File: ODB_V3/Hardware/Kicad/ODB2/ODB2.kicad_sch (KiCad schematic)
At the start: 95 parts, among them U1 STM32F412ZGTx, Y1 ABM8G-25.000MHZ-18-D2Y-T

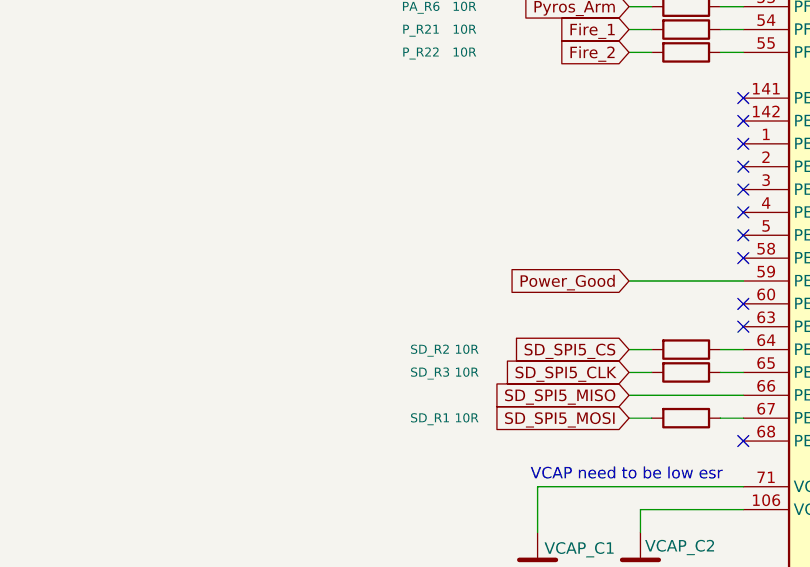
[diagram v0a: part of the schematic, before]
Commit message: feat: add good power input to stm32 + add pull-up 3v3 to good power
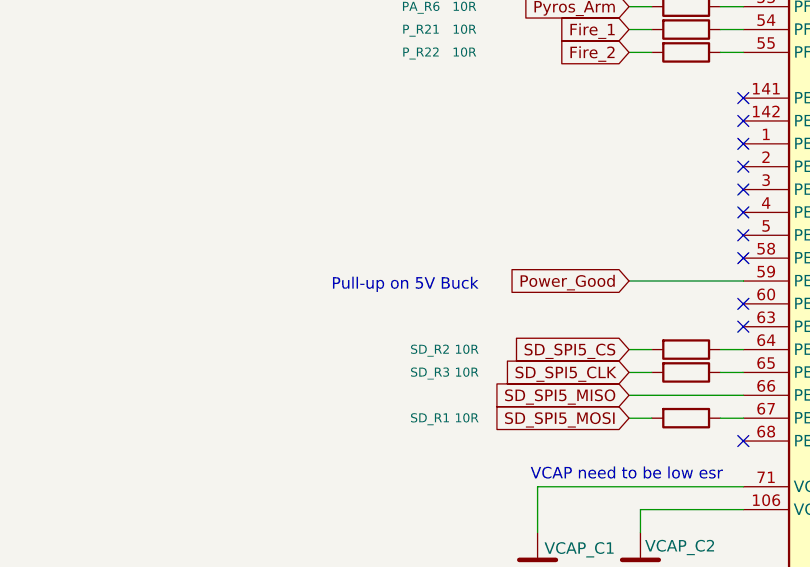
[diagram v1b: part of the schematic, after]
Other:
- note added: "Pull-up on 5V Buck"
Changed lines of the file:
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@@
+		)
+	)
+	(text "Pull-up on 5V Buck"
+		(exclude_from_sim no)
+		(at 132.588 191.008 0)
+		(effects
+			(font
+				(size 1.27 1.27)
+			)
 		)
 	)

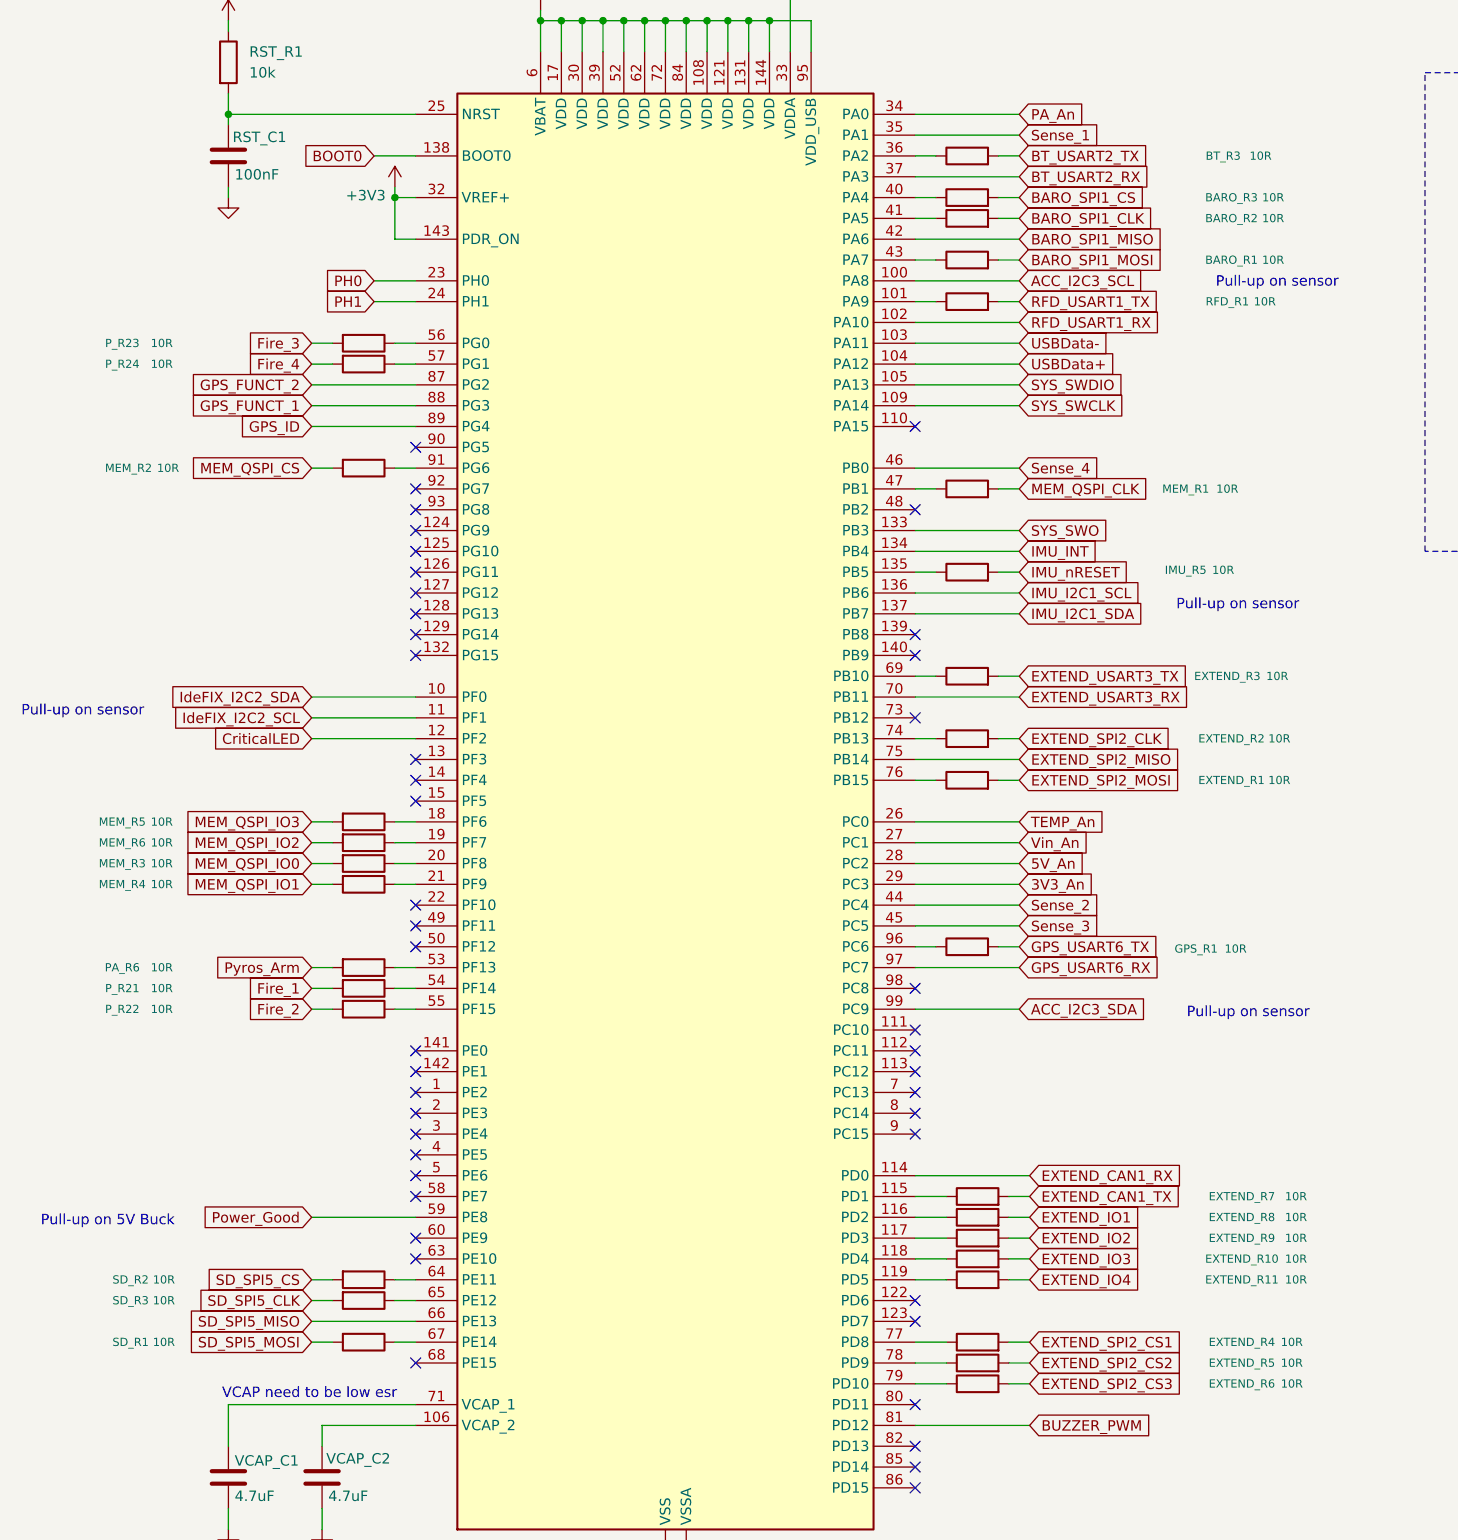
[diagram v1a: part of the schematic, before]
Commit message: fix: reoganised components on pcb
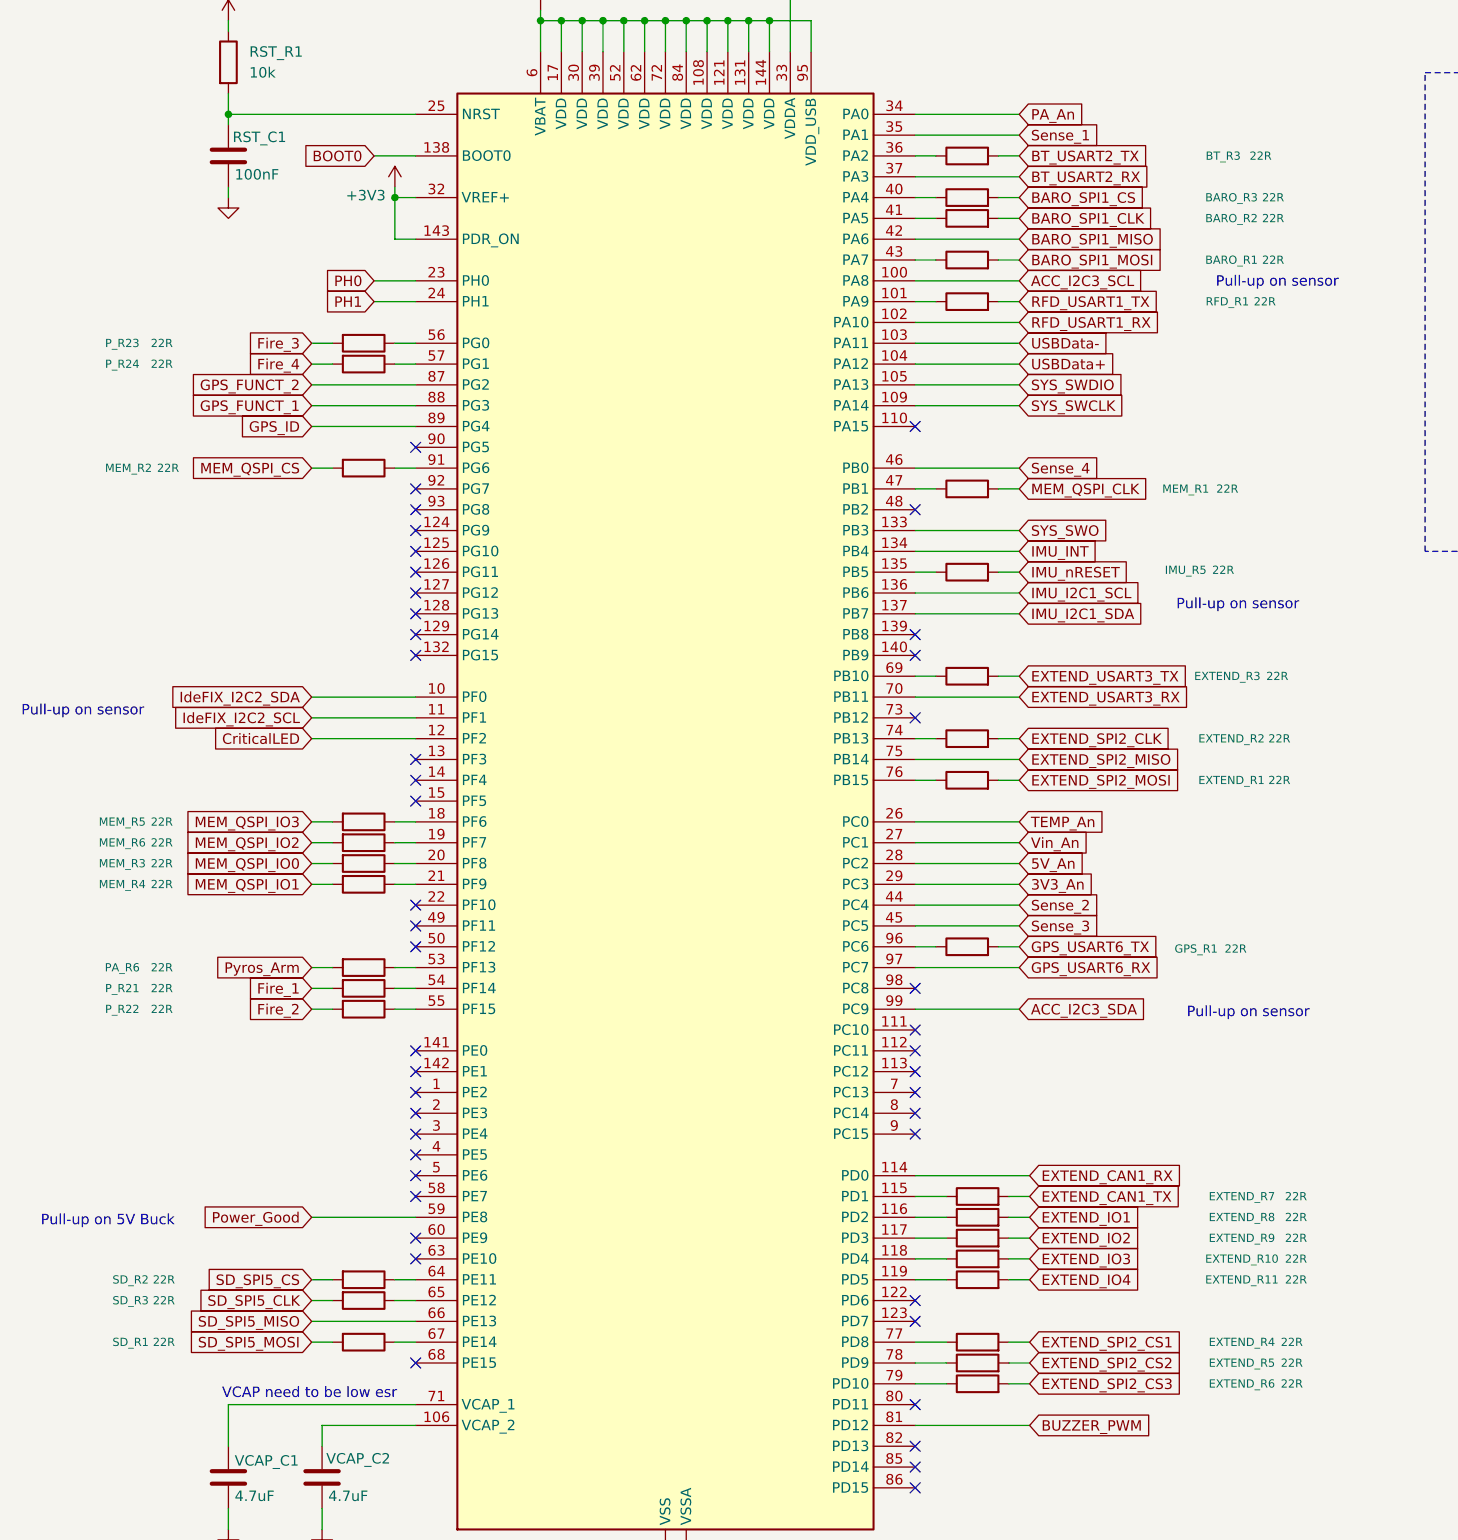
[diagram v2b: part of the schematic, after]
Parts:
- BARO_R1, BARO_R2, BARO_R3, BT_R3, EXTEND_R1, EXTEND_R10, EXTEND_R11, EXTEND_R2, EXTEND_R3, EXTEND_R4, EXTEND_R5, EXTEND_R6, EXTEND_R7, EXTEND_R8, EXTEND_R9, GPS_R1, IMU_R5, MEM_R1, MEM_R2, MEM_R3, MEM_R4, MEM_R5, MEM_R6, PA_R6, P_R21, P_R22, P_R23, P_R24, RFD_R1, SD_R1, SD_R2, SD_R3: value 10R -> 22R
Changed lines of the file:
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@@
 			)
 		)
-		(property "Value" "10R"
+		(property "Value" "22R"
 			(at 139.192 160.02 90)
 			(effects
@@
 			)
 		)
-		(property "Value" "10R"
+		(property "Value" "22R"
 			(at 277.622 187.96 90)
 			(effects
@@
 			)
 		)
-		(property "Value" "10R"
+		(property "Value" "22R"
 			(at 139.192 162.56 90)
 			(effects
@@
 			)
 		)
-		(property "Value" "10R"
+		(property "Value" "22R"
 			(at 274.828 68.58 90)
 			(effects
@@
 			)
 		)
-		(property "Value" "10R"
+		(property "Value" "22R"
 			(at 277.622 198.12 90)
 			(effects
@@
 			)
 		)
-		(property "Value" "10R"
+		(property "Value" "22R"
 			(at 268.732 111.506 90)
 			(effects
@@
 			)
 		)
-		(property "Value" "10R"
+		(property "Value" "22R"
 			(at 139.192 165.1 90)
 			(effects
@@
 			)
 		)
-		(property "Value" "10R"
+		(property "Value" "22R"
 			(at 274.828 73.66 90)
 			(effects
@@
 			)
 		)
-		(property "Value" "10R"
+		(property "Value" "22R"
 			(at 270.256 157.734 90)
 			(effects
@@
 			)
 		)
-		(property "Value" "10R"
+		(property "Value" "22R"
 			(at 139.446 198.12 90)
 			(effects
@@
 			)
 		)
-		(property "Value" "10R"
+		(property "Value" "22R"
 			(at 277.114 210.82 90)
 			(effects
@@
 			)
 		)
-		(property "Value" "10R"
+		(property "Value" "22R"
 			(at 139.192 149.86 90)
 			(effects
@@
 			)
 		)
-		(property "Value" "10R"
+		(property "Value" "22R"
 			(at 139.192 142.24 90)
 			(effects
@@
 			)
 		)
-		(property "Value" "10R"
+		(property "Value" "22R"
 			(at 275.59 137.16 90)
 			(effects
@@
 			)
 		)
-		(property "Value" "10R"
+		(property "Value" "22R"
 			(at 273.304 60.96 90)
 			(effects
@@
 			)
 		)
-		(property "Value" "10R"
+		(property "Value" "22R"
 			(at 277.114 208.28 90)
 			(effects
@@
 			)
 		)
-		(property "Value" "10R"
+		(property "Value" "22R"
 			(at 139.192 83.82 90)
 			(effects
@@
 			)
 		)
-		(property "Value" "10R"
+		(property "Value" "22R"
 			(at 139.192 144.78 90)
 			(effects
@@
 			)
 		)
-		(property "Value" "10R"
+		(property "Value" "22R"
 			(at 139.446 200.66 90)
 			(effects
@@
 			)
 		)
-		(property "Value" "10R"
+		(property "Value" "22R"
 			(at 139.192 86.36 90)
 			(effects
@@
 			)
 		)
-		(property "Value" "10R"
+		(property "Value" "22R"
 			(at 275.336 124.46 90)
 			(effects
@@
 			)
 		)
-		(property "Value" "10R"
+		(property "Value" "22R"
 			(at 139.954 99.06 90)
 			(effects
@@
 			)
 		)
-		(property "Value" "10R"
+		(property "Value" "22R"
 			(at 277.622 190.5 90)
 			(effects
@@
 			)
 		)
-		(property "Value" "10R"
+		(property "Value" "22R"
 			(at 139.192 147.32 90)
 			(effects
@@
 			)
 		)
-		(property "Value" "10R"
+		(property "Value" "22R"
 			(at 274.828 66.04 90)
 			(effects
@@
 			)
 		)
-		(property "Value" "10R"
+		(property "Value" "22R"
 			(at 139.446 205.74 90)
 			(effects
@@
 			)
 		)
-		(property "Value" "10R"
+		(property "Value" "22R"
 			(at 277.114 205.74 90)
 			(effects
@@
 			)
 		)
-		(property "Value" "10R"
+		(property "Value" "22R"
 			(at 277.622 193.04 90)
 			(effects
@@
 			)
 		)
-		(property "Value" "10R"
+		(property "Value" "22R"
 			(at 275.59 132.08 90)
 			(effects
@@
 			)
 		)
-		(property "Value" "10R"
+		(property "Value" "22R"
 			(at 269.24 101.6 90)
 			(effects
@@
 			)
 		)
-		(property "Value" "10R"
+		(property "Value" "22R"
 			(at 277.622 195.58 90)
 			(effects
@@
 			)
 		)
-		(property "Value" "10R"
+		(property "Value" "22R"
 			(at 273.812 78.74 90)
 			(effects
